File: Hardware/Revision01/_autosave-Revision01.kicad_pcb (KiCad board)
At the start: 4 copper layers, 100 x 110.1 mm, 90 parts, among them J10 StrainConn, J11 StrainConn, J12 StrainConn, J14 Conn_01x05, J2 Conn_01x02, J3 Conn_01x02, J4 Battery connector, J5 StrainConn, J6 StrainConn, J7 StrainConn, J8 StrainConn, J9 StrainConn, Q1 PMOS, Q2 NMOS, Q3 PMOS, SW1 ON/OFF_SW_SPST_LED, U1 NUCLEO-L476RG, U2 MRF89XAM9AT-I/RM, U3 ICM-45605

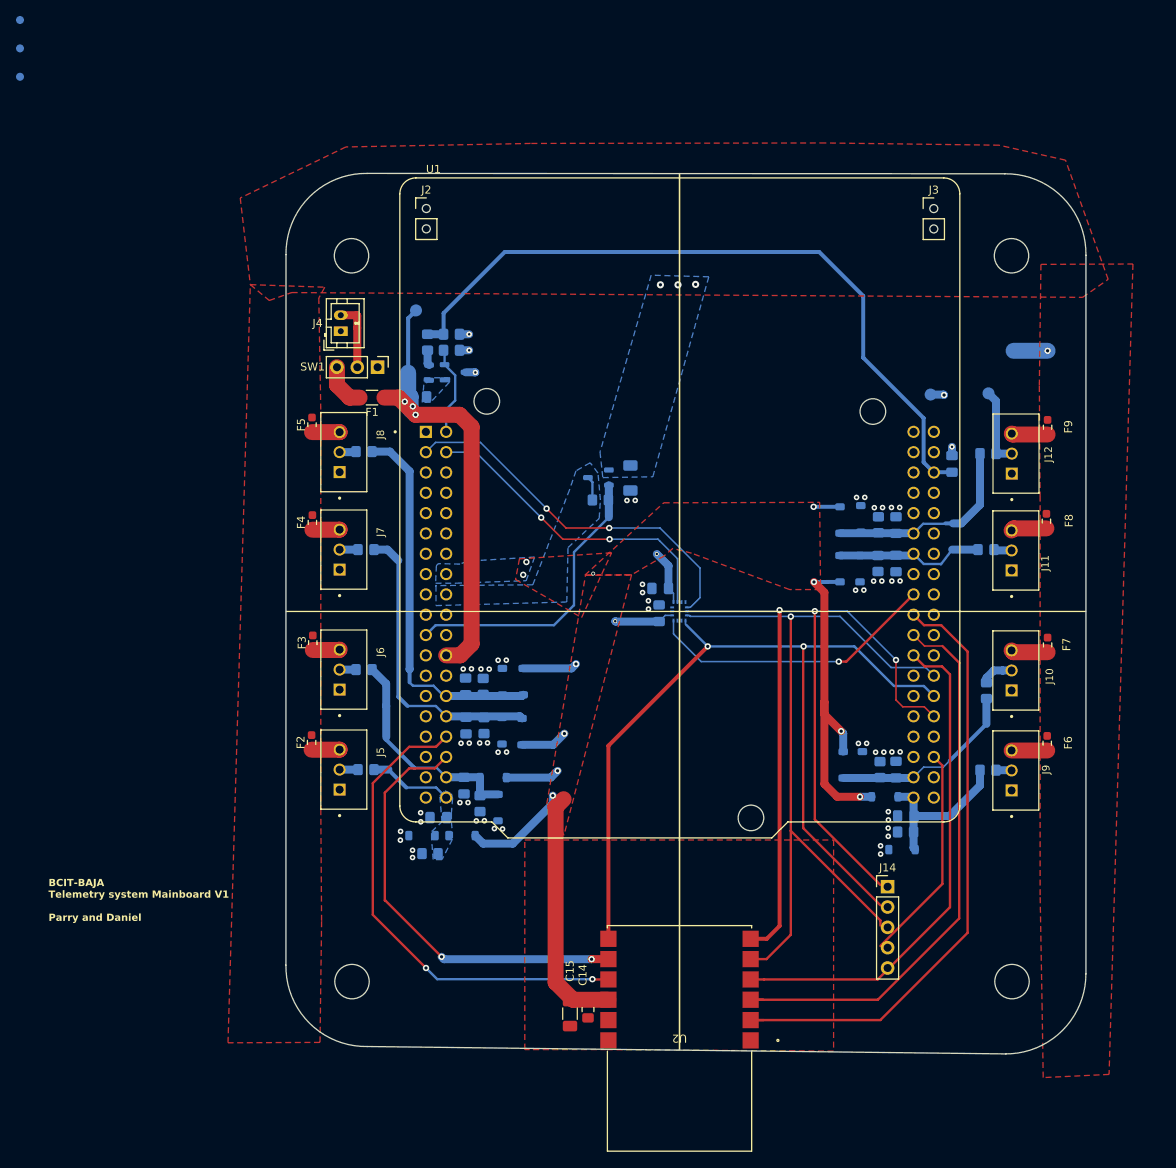
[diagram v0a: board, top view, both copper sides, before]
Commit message: redid ROUTING. Need to redefine layer stackup and stitching via length
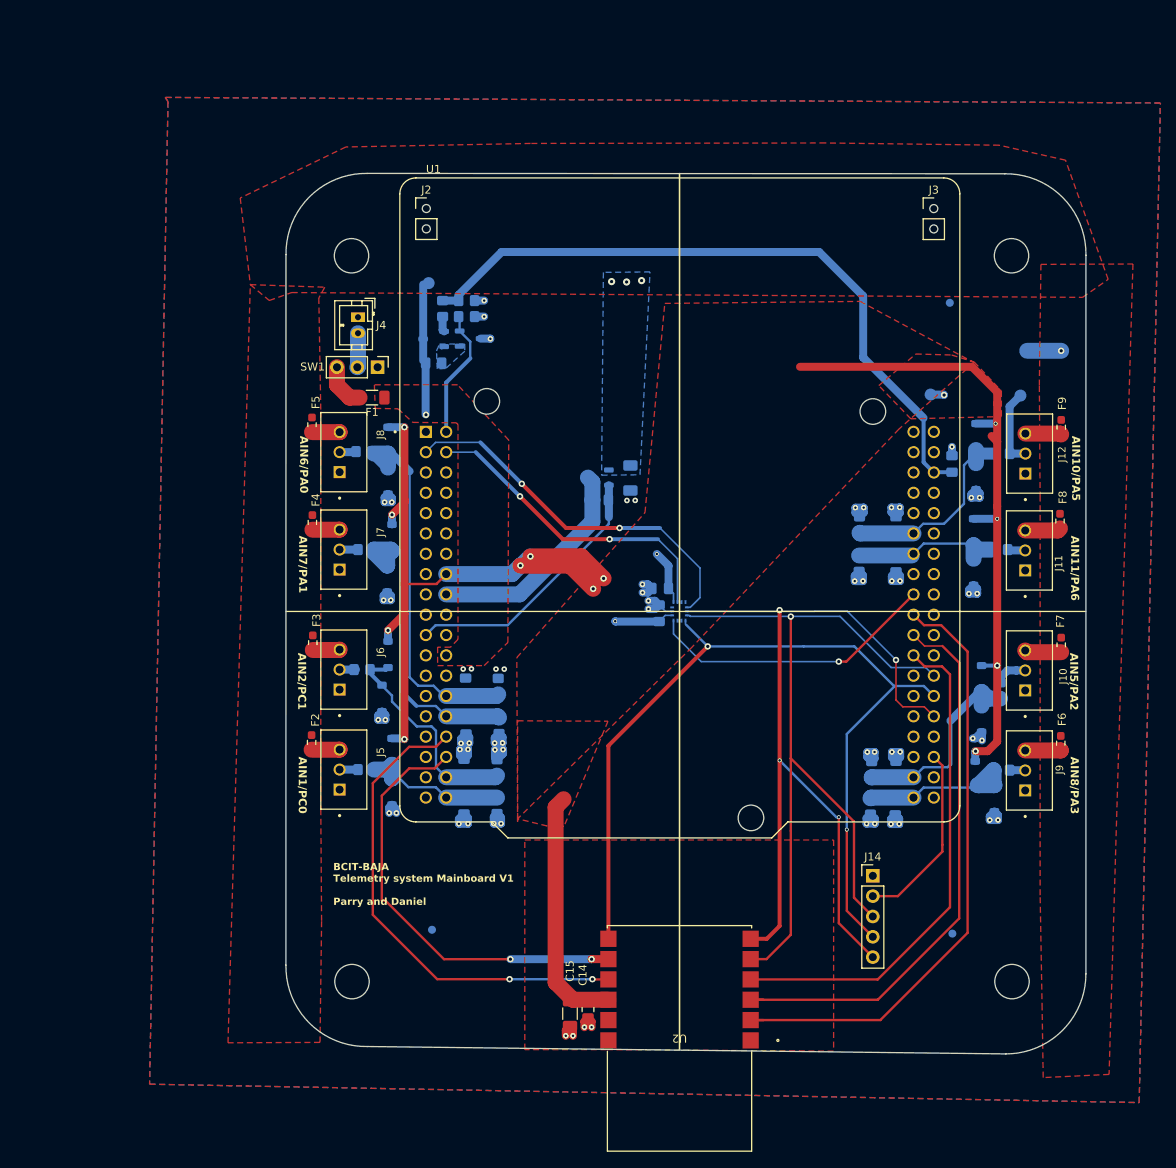
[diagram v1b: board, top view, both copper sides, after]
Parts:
- moved FID2 160.7 mm to (194.3, 137.7)
- moved FID1 121.5 mm to (194.0, 58.8)
- moved FID3 118.4 mm to (129.3, 137.2)
- moved D7 34.6 mm to (123.8, 76.0)
- moved D5 29.2 mm to (124.3, 88.2), turned to -90 degrees
- moved D8 28.9 mm to (123.8, 81.1), turned to -90 degrees
- moved D6 23.8 mm to (123.7, 93.3)
- moved D11 20.4 mm to (198.0, 105.8)
- moved D3 20.3 mm to (123.8, 102.8), turned to -90 degrees
- moved D15 19.9 mm to (197.3, 75.6)
- moved D4 19.9 mm to (123.0, 108.3)
- moved D13 17.3 mm to (197.0, 87.5), turned to -90 degrees
- moved D12 16.0 mm to (198.0, 110.8), turned to -90 degrees
- moved D16 15.3 mm to (197.3, 80.5), turned to -90 degrees
- moved D14 14.2 mm to (197.0, 92.5)
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- renumbered TP10 to +StrainV, TP3 to +Vbatt, TP9 to AIN10, TP8 to GND
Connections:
- U1 pad CN10_19: /ANT_IRQ0_GPIO -> /ANT_RESET_ANT_GPIO
- U1 pad CN10_23: /ANT_RESET_ANT_GPIO -> /ANT_IRQ0_GPIO
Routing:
- net GND: track 6.44 -> 99.3 mm, vias 59 -> 63
- net +3.3V: track 124.0 -> 216.1 mm, vias 13 -> 14
- net +V_batt: track 57.2 -> 17.2 mm, vias 3 -> 1
- net /PC5_AIN2_14_BATT_V: track 90.5 -> 125.1 mm
- net +5V: track 3.03 -> 27.8 mm
- net /AIN1_6: track 47.1 -> 56.5 mm
- net /AIN1_1: track 10.5 -> 19.7 mm
- net /PB13_SPI2_SCK: track 120.7 -> 112.7 mm, vias 3 -> 4
- net /PB15_SPI2_MOSI: track 96.6 -> 104.1 mm
- net /BatteryV_Div_Enable_GPIO: track 11.3 -> 16.3 mm
- net Net-(BT1-+): track 8.52 -> 4.29 mm
- net /~{CANBUS_CS_GPIO}: track 27.3 -> 23.6 mm
- net /StrainV_Enable_GPIO: track 36.9 -> 33.5 mm
- net /AIN1_10: track 25.2 -> 27.9 mm
- net /AIN1_7: track 37.2 -> 39.2 mm
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- added copper zone on F.Cu, net +V_batt
- added copper zone on B.Cu, net GND
- removed copper zone on B.Cu, net +3.3V
- removed copper zone on B.Cu, net +5V
- removed copper zone on B.Cu, net /AIN1_1
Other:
- board text added: "AIN1/PC0"
- board text added: "AIN10/PA5"
- board text added: "AIN11/PA6"
- board text added: "AIN2/PC1"
- board text added: "AIN5/PA2"
- board text added: "AIN6/PA0"
- board text added: "AIN7/PA1"
- board text added: "AIN8/PA3"
